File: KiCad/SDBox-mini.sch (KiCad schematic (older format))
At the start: 10 parts, among them J1 DB25_Male, J2 Micro_SD_Card, U1 ATmega328P-AU, Y1 Crystal_GND24_Small

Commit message: added 3V3 voltage regulator, added 74LVC125A buffer
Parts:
- added C1, C2: 10uF, Capacitor_SMD:C_1206_3216Metric_Pad1.42x1.75mm_HandSolder, symbol Device:C_Small
- added C3, C9: 0.1uF, Capacitor_SMD:C_0603_1608Metric_Pad1.05x0.95mm_HandSolder, symbol Device:C_Small
- added R2: 10k, Resistor_SMD:R_0603_1608Metric_Pad1.05x0.95mm_HandSolder, symbol Device:R_Small
- added U2: LM1117-3.3, Package_TO_SOT_SMD:SOT-223, symbol Regulator_Linear:LM1117-3.3
- added U3: 74LVC125A, Package_SO:TSSOP-14_4.4x5mm_P0.65mm, symbol SDBox-mini:74LVC125A
- Y1: footprint Oscillator:Oscillator_SMD_Fordahl_DFAS15-4Pin_5.0x3.2mm_HandSoldering -> SDBox-mini:Crystal_EuroQuartz_SMD_4Pin_5.0x3.2mm
- renumbered C1 to C4, C2 to C5, C3 to C6, C4 to C7, C5 to C8
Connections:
- net labels added: MISO_3V3, MOSI_3V3, SCK_3V3, SELECT_3V3
- net labels removed: CS
- wire segments 32 -> 37
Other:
- moved on the sheet: J1
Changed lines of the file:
@@
 $EndDescr
 $Comp
-L Device:C_Small C2
+L Device:C_Small C5
 U 1 1 606A3110
 P 3000 1600
-F 0 "C2" V 2850 1750 50  0000 R CNN
+F 0 "C5" V 2850 1750 50  0000 R CNN
 F 1 "0.1uF" V 2850 1400 50  0000 L CNN
 F 2 "Capacitor_SMD:C_0603_1608Metric_Pad1.05x0.95mm_HandSolder" H 3000 1600 50  0001 C CNN
@@
 L Connector:DB25_Male J1
 U 1 1 60F40974
-P 2500 2750
-F 0 "J1" V 2817 2750 50  0000 C CNN
-F 1 "DB25_Male" V 2726 2750 50  0000 C CNN
-F 2 "Connector_Dsub:DSUB-25_Male_EdgeMount_P2.77mm" H 2500 2750 50  0001 C CNN
-F 3 " ~" H 2500 2750 50  0001 C CNN
-	1    2500 2750
-	1    0    0    -1
-$EndComp
-Text GLabel 2200 1550 0    50   BiDi ~ 0
+P 2300 2750
+F 0 "J1" V 2617 2750 50  0000 C CNN
+F 1 "DB25_Male" V 2526 2750 50  0000 C CNN
+F 2 "Connector_Dsub:DSUB-25_Male_EdgeMount_P2.77mm" H 2300 2750 50  0001 C CNN
+F 3 " ~" H 2300 2750 50  0001 C CNN
+	1    2300 2750
+	1    0    0    -1
+$EndComp
+Text GLabel 2000 1550 0    50   BiDi ~ 0
 SELECT
-NoConn ~ 2200 1650
-NoConn ~ 2200 1850
-NoConn ~ 2200 2050
-Text GLabel 2200 1750 0    50   BiDi ~ 0
+NoConn ~ 2000 1650
+NoConn ~ 2000 1850
+NoConn ~ 2000 2050
+Text GLabel 2000 1750 0    50   BiDi ~ 0
 POUT
-Text GLabel 2200 1950 0    50   BiDi ~ 0
+Text GLabel 2000 1950 0    50   BiDi ~ 0
 BUSY
-Text GLabel 1850 2750 0    50   Input ~ 0
-GND
-Wire Wire Line
-	1850 2250 1850 2450
-Connection ~ 1850 2450
-Wire Wire Line
-	1850 2450 1850 2650
-Wire Wire Line
-	1850 3050 1850 2850
-Connection ~ 1850 2650
-Connection ~ 1850 2850
-Wire Wire Line
-	1850 2850 1850 2650
-Text GLabel 2200 2350 0    50   BiDi ~ 0
+Text GLabel 1650 2750 0    50   Input ~ 0
+GND
+Wire Wire Line
+	1650 2250 1650 2450
+Connection ~ 1650 2450
+Wire Wire Line
+	1650 2450 1650 2650
+Wire Wire Line
+	1650 3050 1650 2850
+Connection ~ 1650 2650
+Connection ~ 1650 2850
+Wire Wire Line
+	1650 2850 1650 2650
+Text GLabel 2000 2350 0    50   BiDi ~ 0
 D7
-Text GLabel 2200 2550 0    50   BiDi ~ 0
+Text GLabel 2000 2550 0    50   BiDi ~ 0
 D6
-Text GLabel 2200 2750 0    50   BiDi ~ 0
+Text GLabel 2000 2750 0    50   BiDi ~ 0
 D5
-Text GLabel 2200 2950 0    50   BiDi ~ 0
+Text GLabel 2000 2950 0    50   BiDi ~ 0
 D4
-Text GLabel 2200 3150 0    50   BiDi ~ 0
+Text GLabel 2000 3150 0    50   BiDi ~ 0
 D3
 Wire Wire Line
-	1850 3250 1850 3050
-Connection ~ 1850 3050
-Wire Wire Line
-	1850 2250 2200 2250
-Wire Wire Line
-	1850 2450 2200 2450
-Wire Wire Line
-	1850 2650 2200 2650
-Wire Wire Line
-	1850 2850 2200 2850
-Wire Wire Line
-	1850 3050 2200 3050
-Wire Wire Line
-	1850 3250 2200 3250
-Text GLabel 2200 3350 0    50   BiDi ~ 0
+	1650 3250 1650 3050
+Connection ~ 1650 3050
+Wire Wire Line
+	1650 2250 2000 2250
+Wire Wire Line
+	1650 2450 2000 2450
+Wire Wire Line
+	1650 2650 2000 2650
+Wire Wire Line
+	1650 2850 2000 2850
+Wire Wire Line
+	1650 3050 2000 3050
+Wire Wire Line
+	1650 3250 2000 3250
+Text GLabel 2000 3350 0    50   BiDi ~ 0
 D2
-Text GLabel 2200 3450 0    50   Output ~ 0
+Text GLabel 2000 3450 0    50   Output ~ 0
 RESET
-Text GLabel 2200 3550 0    50   BiDi ~ 0
+Text GLabel 2000 3550 0    50   BiDi ~ 0
 D1
-NoConn ~ 2200 3650
-Text GLabel 2200 3750 0    50   BiDi ~ 0
+NoConn ~ 2000 3650
+Text GLabel 2000 3750 0    50   BiDi ~ 0
 D0
 $Comp
@@
 	-1   0    0    1
 $EndComp
-NoConn ~ 2200 3850
+NoConn ~ 2000 3850
 Text GLabel 4950 2800 1    50   Input ~ 0
 VCC
@@
 F 0 "Y1" V 5300 2200 50  0000 L CNN
 F 1 "Crystal_GND24_Small" V 5500 2400 50  0001 L CNN
-F 2 "Oscillator:Oscillator_SMD_Fordahl_DFAS15-4Pin_5.0x3.2mm_HandSoldering" H 5300 2250 50  0001 C CNN
+F 2 "SDBox-mini:Crystal_EuroQuartz_SMD_4Pin_5.0x3.2mm" H 5300 2250 50  0001 C CNN
 F 3 "~" H 5300 2250 50  0001 C CNN
 	1    5300 2250
@@
 GND
 $Comp
-L Device:C_Small C4
+L Device:C_Small C7
 U 1 1 60FA06FB
 P 5550 2100
-F 0 "C4" V 5650 2250 50  0000 R CNN
+F 0 "C7" V 5650 2250 50  0000 R CNN
 F 1 "16pF" V 5650 1900 50  0000 L CNN
 F 2 "Capacitor_SMD:C_0603_1608Metric_Pad1.05x0.95mm_HandSolder" H 5550 2100 50  0001 C CNN
@@
 	4900 2100 5300 2100
 $Comp
-L Device:C_Small C5
+L Device:C_Small C8
 U 1 1 60FA5116
 P 5550 2400
-F 0 "C5" V 5450 2550 50  0000 R CNN
+F 0 "C8" V 5450 2550 50  0000 R CNN
 F 1 "16pF" V 5450 2200 50  0000 L CNN
 F 2 "Capacitor_SMD:C_0603_1608Metric_Pad1.05x0.95mm_HandSolder" H 5550 2400 50  0001 C CNN
@@
 Connection ~ 5650 2250
 $Comp
-L Device:C_Small C3
+L Device:C_Small C6
 U 1 1 60FA7C64
 P 3700 1250
-F 0 "C3" V 3800 1400 50  0000 R CNN
+F 0 "C6" V 3800 1400 50  0000 R CNN
 F 1 "0.1uF" V 3800 1050 50  0000 L CNN
 F 2 "Capacitor_SMD:C_0603_1608Metric_Pad1.05x0.95mm_HandSolder" H 3700 1250 50  0001 C CNN
@@
 Text GLabel 4550 3400 2    50   Output ~ 0
 TXO
-NoConn ~ 2200 2150
-NoConn ~ 2200 3950
+NoConn ~ 2000 2150
+NoConn ~ 2000 3950
 Text GLabel 4550 2000 2    50   Input ~ 0
 MISO
@@
 DTR
 $Comp
-L Device:C_Small C1
+L Device:C_Small C4
 U 1 1 60F8E9CC
 P 5350 3100
-F 0 "C1" V 5200 3250 50  0000 R CNN
+F 0 "C4" V 5200 3250 50  0000 R CNN
 F 1 "0.1uF" V 5200 2900 50  0000 L CNN
 F 2 "Capacitor_SMD:C_0603_1608Metric_Pad1.05x0.95mm_HandSolder" H 5350 3100 50  0001 C CNN
@@
 $EndComp
 NoConn ~ 7900 2350
-Text GLabel 7900 1750 2    50   Output ~ 0
+Text GLabel 7450 4800 2    50   Output ~ 0
 MISO
 Text GLabel 7900 1850 2    50   Input ~ 0
 GND
-Text GLabel 7900 1950 2    50   Input ~ 0
+Text GLabel 6550 3800 0    50   Input ~ 0
 SCK
 Text GLabel 7900 2050 2    50   Input ~ 0
 3V3
-Text GLabel 7900 2150 2    50   Input ~ 0
+Text GLabel 6550 3300 0    50   Input ~ 0
 MOSI
 NoConn ~ 7900 1650
 NoConn ~ 6200 1450
 Text GLabel 7900 2250 2    50   Input ~ 0
-CS
+SELECT_3V3
+$Comp
+L SDBox-mini:74LVC125A U3
+U 1 1 60FFE391
+P 7000 4150
+F 0 "U3" H 7000 5565 50  0000 C CNN
+F 1 "74LVC125A" H 7000 5474 50  0000 C CNN
+F 2 "Package_SO:TSSOP-14_4.4x5mm_P0.65mm" H 8200 5200 50  0001 C CNN
+F 3 "https://assets.nexperia.com/documents/data-sheet/74LVC125A.pdf" H 8200 5200 50  0001 C CNN
+	1    7000 4150
+	1    0    0    -1
+$EndComp
+Text GLabel 6550 3550 0    50   Input ~ 0
+GND
+Text GLabel 6550 4050 0    50   Input ~ 0
+GND
+Text GLabel 6550 4550 0    50   Input ~ 0
+GND
+Text GLabel 6550 5050 0    50   Input ~ 0
+GND
+Text GLabel 6550 4300 0    50   Input ~ 0
+SELECT
+Text GLabel 7450 4300 2    50   Output ~ 0
+SELECT_3V3
+Text GLabel 7450 4050 2    50   Input ~ 0
+GND
+$Comp
+L Device:C_Small C9
+U 1 1 61017825
+P 7450 5150
+F 0 "C9" H 7350 5150 50  0000 R CNN
+F 1 "0.1uF" H 7200 5250 50  0000 L CNN
+F 2 "Capacitor_SMD:C_0603_1608Metric_Pad1.05x0.95mm_HandSolder" H 7450 5150 50  0001 C CNN
+F 3 "~" H 7450 5150 50  0001 C CNN
+	1    7450 5150
+	-1   0    0    1
+$EndComp
+Text GLabel 7450 5250 3    50   Input ~ 0
+GND
+Text GLabel 7450 5050 2    50   Input ~ 0
+VCC
+$Comp
+L Device:R_Small R2
+U 1 1 6101E2BD
+P 6000 4700
+F 0 "R2" H 5941 4654 50  0000 R CNN
+F 1 "10k" H 5941 4745 50  0000 R CNN
+F 2 "Resistor_SMD:R_0603_1608Metric_Pad1.05x0.95mm_HandSolder" H 6000 4700 50  0001 C CNN
+F 3 "~" H 6000 4700 50  0001 C CNN
+	1    6000 4700
+	-1   0    0    1
+$EndComp
+Text GLabel 6000 4600 1    50   Input ~ 0
+3V3
+Text GLabel 7900 2150 2    50   Input ~ 0
+MOSI_3V3
+Text GLabel 7450 3300 2    50   Output ~ 0
+MOSI_3V3
+Text GLabel 7900 1750 2    50   Output ~ 0
+MISO_3V3
+Text GLabel 5700 4800 0    50   Input ~ 0
+MISO_3V3
+Wire Wire Line
+	5700 4800 6000 4800
+Connection ~ 6000 4800
+Wire Wire Line
+	6000 4800 6550 4800
+Text GLabel 7450 3800 2    50   Output ~ 0
+SCK_3V3
+Text GLabel 7900 1950 2    50   Input ~ 0
+SCK_3V3
+$Comp
+L Regulator_Linear:LM1117-3.3 U2
+U 1 1 61034FEA
+P 9550 1750
+F 0 "U2" H 9550 1992 50  0000 C CNN
+F 1 "LM1117-3.3" H 9550 1901 50  0000 C CNN
+F 2 "Package_TO_SOT_SMD:SOT-223" H 9550 1750 50  0001 C CNN
+F 3 "http://www.ti.com/lit/ds/symlink/lm1117.pdf" H 9550 1750 50  0001 C CNN
+	1    9550 1750
+	1    0    0    -1
+$EndComp
+Text GLabel 9250 1750 0    50   Input ~ 0
+VCC
+$Comp
+L Device:C_Small C1
+U 1 1 610421CE
+P 9250 1650
+F 0 "C1" H 9450 1650 50  0000 R CNN
+F 1 "10uF" H 9300 1550 50  0000 L CNN
+F 2 "Capacitor_SMD:C_1206_3216Metric_Pad1.42x1.75mm_HandSolder" H 9250 1650 50  0001 C CNN
+F 3 "~" H 9250 1650 50  0001 C CNN
+	1    9250 1650
+	-1   0    0    1
+$EndComp
+$Comp
+L Device:C_Small C2
+U 1 1 610444D0
+P 9850 1650
+F 0 "C2" H 9750 1650 50  0000 R CNN
+F 1 "10uF" H 9600 1550 50  0000 L CNN
+F 2 "Capacitor_SMD:C_1206_3216Metric_Pad1.42x1.75mm_HandSolder" H 9850 1650 50  0001 C CNN
+F 3 "~" H 9850 1650 50  0001 C CNN
+	1    9850 1650
+	-1   0    0    1
+$EndComp
+Text GLabel 9250 1550 1    50   Input ~ 0
+GND
+Text GLabel 9850 1550 1    50   Input ~ 0
+GND
+$Comp
+L Device:C_Small C3
+U 1 1 6104580B
+P 10200 1650
+F 0 "C3" H 10100 1650 50  0000 R CNN
+F 1 "0.1uF" H 9950 1550 50  0000 L CNN
+F 2 "Capacitor_SMD:C_0603_1608Metric_Pad1.05x0.95mm_HandSolder" H 10200 1650 50  0001 C CNN
+F 3 "~" H 10200 1650 50  0001 C CNN
+	1    10200 1650
+	-1   0    0    1
+$EndComp
+Text GLabel 10200 1550 1    50   Input ~ 0
+GND
+Wire Wire Line
+	9850 1750 10200 1750
+Connection ~ 9850 1750
+Wire Wire Line
+	9850 1850 9850 1750
+Text GLabel 9550 2050 3    50   Input ~ 0
+GND
+Text GLabel 10350 1750 2    50   Output ~ 0
+3V3
+Wire Wire Line
+	10200 1750 10350 1750
+Connection ~ 10200 1750
 $EndSCHEMATC

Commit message: added FTDI header
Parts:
- added J2: Conn_01x06, Connector_PinHeader_2.54mm:PinHeader_1x06_P2.54mm_Vertical, symbol Connector_Generic:Conn_01x06
- renumbered J2 to J3
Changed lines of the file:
@@
 NoConn ~ 4550 1800
 $Comp
-L Connector:Micro_SD_Card J2
+L Connector:Micro_SD_Card J3
 U 1 1 60FD5546
 P 7000 2050
-F 0 "J2" H 6950 1233 50  0000 C CNN
+F 0 "J3" H 6950 1233 50  0000 C CNN
 F 1 "Micro_SD_Card" H 6950 1324 50  0000 C CNN
 F 2 "SDBox-mini:GCT-MEM2055-00-190-01-A" H 8150 2350 50  0001 C CNN
@@
 GND
 Text GLabel 7450 5050 2    50   Input ~ 0
-VCC
+3V3
 $Comp
 L Device:R_Small R2
@@
 	10200 1750 10350 1750
 Connection ~ 10200 1750
+$Comp
+L Connector_Generic:Conn_01x06 J2
+U 1 1 6104A5C2
+P 2200 5000
+F 0 "J2" H 2118 4475 50  0000 C CNN
+F 1 "Conn_01x06" H 2118 4566 50  0000 C CNN
+F 2 "Connector_PinHeader_2.54mm:PinHeader_1x06_P2.54mm_Vertical" H 2200 5000 50  0001 C CNN
+F 3 "~" H 2200 5000 50  0001 C CNN
+	1    2200 5000
+	-1   0    0    1
+$EndComp
+Text GLabel 2400 5200 2    50   Input ~ 0
+DTR
+Text GLabel 2400 5100 2    50   Input ~ 0
+TXO
+Text GLabel 2400 5000 2    50   Output ~ 0
+RXI
+Text GLabel 2400 4900 2    50   Input ~ 0
+VCC
+Text GLabel 2400 4800 2    50   Input ~ 0
+GND
+Text GLabel 2400 4700 2    50   Input ~ 0
+GND
 $EndSCHEMATC

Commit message: changed to 74LVC3G17
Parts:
- removed U3: 74LVC125A, Package_SO:TSSOP-14_4.4x5mm_P0.65mm, symbol SDBox-mini:74LVC125A
- added U3: 74LVC3G17, Package_SO:TSSOP-8_3x3mm_P0.65mm, symbol SDBox-mini:74LVC3G17
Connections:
- wire segments 37 -> 39
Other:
- moved on the sheet: C9, R2
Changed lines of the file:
@@
 $EndComp
 NoConn ~ 7900 2350
-Text GLabel 7450 4800 2    50   Output ~ 0
+Text GLabel 6100 4250 2    50   Output ~ 0
 MISO
 Text GLabel 7900 1850 2    50   Input ~ 0
 GND
-Text GLabel 6550 3800 0    50   Input ~ 0
+Text GLabel 7650 4150 2    50   Input ~ 0
 SCK
 Text GLabel 7900 2050 2    50   Input ~ 0
 3V3
-Text GLabel 6550 3300 0    50   Input ~ 0
+Text GLabel 6850 3450 0    50   Input ~ 0
 MOSI
 NoConn ~ 7900 1650
@@
 Text GLabel 7900 2250 2    50   Input ~ 0
 SELECT_3V3
-$Comp
-L SDBox-mini:74LVC125A U3
-U 1 1 60FFE391
-P 7000 4150
-F 0 "U3" H 7000 5565 50  0000 C CNN
-F 1 "74LVC125A" H 7000 5474 50  0000 C CNN
-F 2 "Package_SO:TSSOP-14_4.4x5mm_P0.65mm" H 8200 5200 50  0001 C CNN
-F 3 "https://assets.nexperia.com/documents/data-sheet/74LVC125A.pdf" H 8200 5200 50  0001 C CNN
-	1    7000 4150
-	1    0    0    -1
-$EndComp
-Text GLabel 6550 3550 0    50   Input ~ 0
+Text GLabel 6800 4500 0    50   Input ~ 0
 GND
-Text GLabel 6550 4050 0    50   Input ~ 0
+Text GLabel 6850 4150 0    50   Input ~ 0
+SELECT
+Text GLabel 7650 4500 2    50   Output ~ 0
+SELECT_3V3
+Text GLabel 7850 3250 1    50   Input ~ 0
 GND
-Text GLabel 6550 4550 0    50   Input ~ 0
-GND
-Text GLabel 6550 5050 0    50   Input ~ 0
-GND
-Text GLabel 6550 4300 0    50   Input ~ 0
-SELECT
-Text GLabel 7450 4300 2    50   Output ~ 0
-SELECT_3V3
-Text GLabel 7450 4050 2    50   Input ~ 0
-GND
-$Comp
-L Device:C_Small C9
-U 1 1 61017825
-P 7450 5150
-F 0 "C9" H 7350 5150 50  0000 R CNN
-F 1 "0.1uF" H 7200 5250 50  0000 L CNN
-F 2 "Capacitor_SMD:C_0603_1608Metric_Pad1.05x0.95mm_HandSolder" H 7450 5150 50  0001 C CNN
-F 3 "~" H 7450 5150 50  0001 C CNN
-	1    7450 5150
-	-1   0    0    1
-$EndComp
-Text GLabel 7450 5250 3    50   Input ~ 0
-GND
-Text GLabel 7450 5050 2    50   Input ~ 0
-3V3
 $Comp
 L Device:R_Small R2
 U 1 1 6101E2BD
-P 6000 4700
-F 0 "R2" H 5941 4654 50  0000 R CNN
-F 1 "10k" H 5941 4745 50  0000 R CNN
-F 2 "Resistor_SMD:R_0603_1608Metric_Pad1.05x0.95mm_HandSolder" H 6000 4700 50  0001 C CNN
-F 3 "~" H 6000 4700 50  0001 C CNN
-	1    6000 4700
+P 5550 4500
+F 0 "R2" H 5491 4454 50  0000 R CNN
+F 1 "10k" H 5491 4545 50  0000 R CNN
+F 2 "Resistor_SMD:R_0603_1608Metric_Pad1.05x0.95mm_HandSolder" H 5550 4500 50  0001 C CNN
+F 3 "~" H 5550 4500 50  0001 C CNN
+	1    5550 4500
 	-1   0    0    1
 $EndComp
-Text GLabel 6000 4600 1    50   Input ~ 0
+Text GLabel 5550 4400 1    50   Input ~ 0
 3V3
 Text GLabel 7900 2150 2    50   Input ~ 0
 MOSI_3V3
-Text GLabel 7450 3300 2    50   Output ~ 0
+Text GLabel 7650 3800 2    50   Output ~ 0
 MOSI_3V3
 Text GLabel 7900 1750 2    50   Output ~ 0
 MISO_3V3
-Text GLabel 5700 4800 0    50   Input ~ 0
+Text GLabel 5250 4600 0    50   Input ~ 0
 MISO_3V3
 Wire Wire Line
-	5700 4800 6000 4800
-Connection ~ 6000 4800
+	5250 4600 5550 4600
+Connection ~ 5550 4600
 Wire Wire Line
-	6000 4800 6550 4800
-Text GLabel 7450 3800 2    50   Output ~ 0
+	5550 4600 6100 4600
+Text GLabel 6850 3800 0    50   Output ~ 0
 SCK_3V3
 Text GLabel 7900 1950 2    50   Input ~ 0
@@
 Text GLabel 2400 4700 2    50   Input ~ 0
 GND
+$Comp
+L Device:C_Small C9
+U 1 1 61017825
+P 7850 3350
+F 0 "C9" H 7700 3250 50  0000 R CNN
+F 1 "0.1uF" H 7500 3350 50  0000 L CNN
+F 2 "Capacitor_SMD:C_0603_1608Metric_Pad1.05x0.95mm_HandSolder" H 7850 3350 50  0001 C CNN
+F 3 "~" H 7850 3350 50  0001 C CNN
+	1    7850 3350
+	-1   0    0    1
+$EndComp
+$Comp
+L SDBox-mini:74LVC3G17 U3
+U 1 1 610573DA
+P 7250 4000
+F 0 "U3" H 7250 4915 50  0000 C CNN
+F 1 "74LVC3G17" H 7250 4824 50  0000 C CNN
+F 2 "Package_SO:TSSOP-8_3x3mm_P0.65mm" H 8100 4400 50  0001 C CNN
+F 3 "http://www.ti.com/lit/sg/scyt129e/scyt129e.pdf" H 8100 4400 50  0001 C CNN
+	1    7250 4000
+	1    0    0    -1
+$EndComp
+Text GLabel 8100 3450 2    50   Input ~ 0
+3V3
+Wire Wire Line
+	8100 3450 7850 3450
+Connection ~ 7850 3450
+Wire Wire Line
+	7850 3450 7700 3450
 $EndSCHEMATC

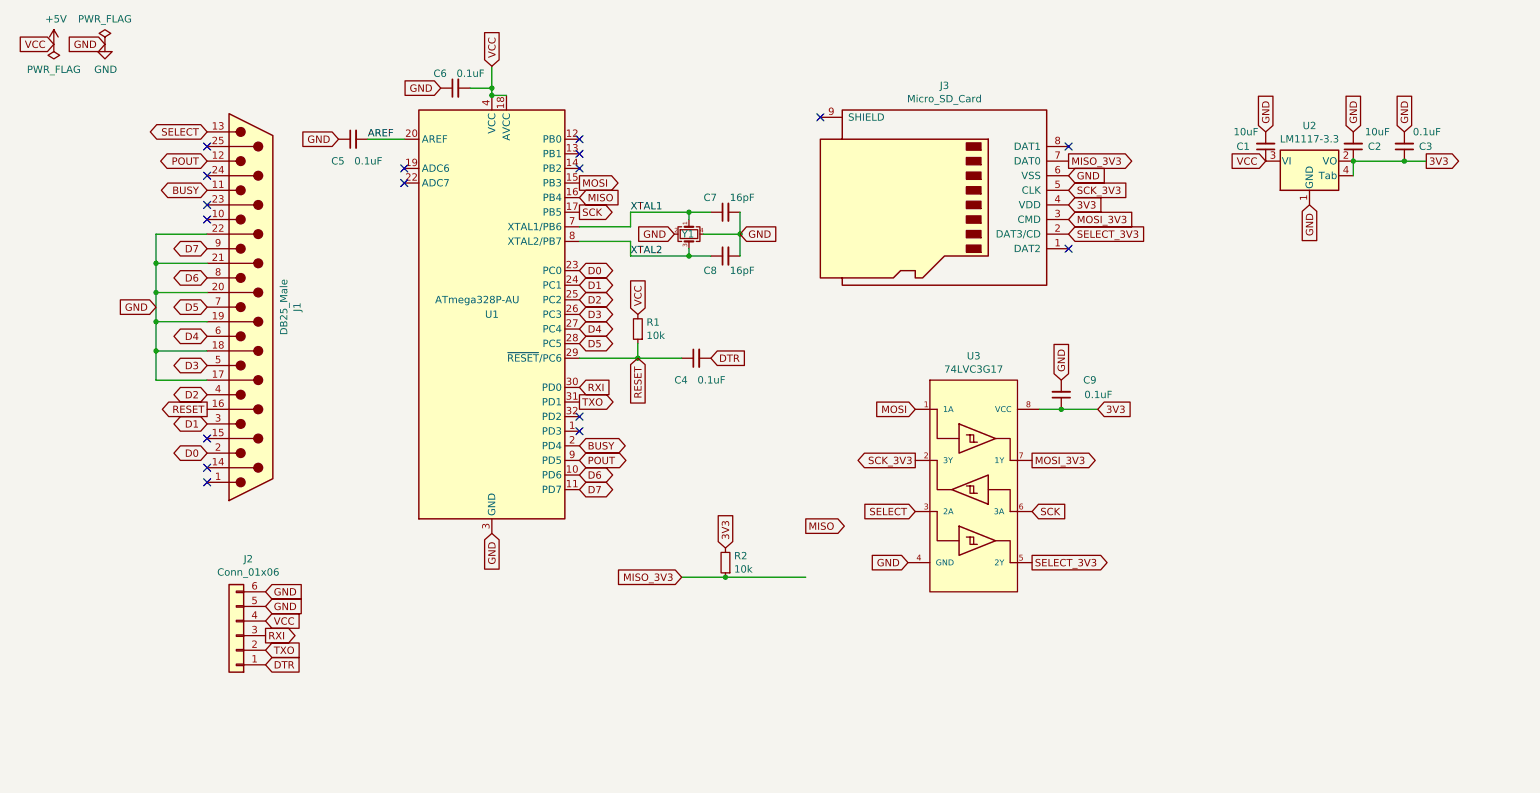
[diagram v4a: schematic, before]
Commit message: added USB micro jack, and Dual non-inverting Schmitt trigger, and debounce circuit for card detect
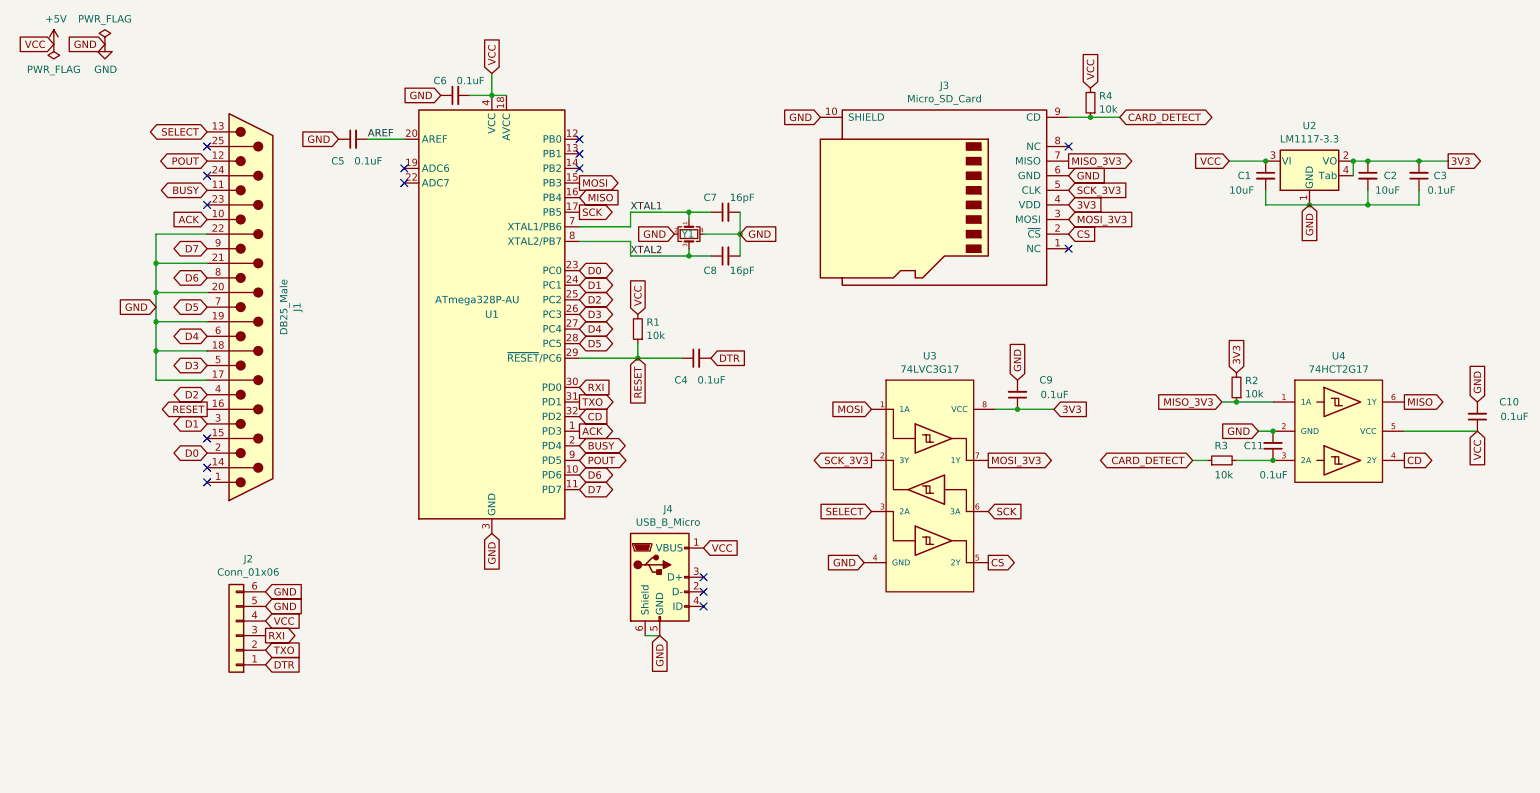
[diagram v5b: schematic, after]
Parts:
- removed J3: Micro_SD_Card, SDBox-mini:GCT-MEM2055-00-190-01-A, symbol Connector:Micro_SD_Card
- added C10, C11: 0.1uF, Capacitor_SMD:C_0603_1608Metric_Pad1.05x0.95mm_HandSolder, symbol Device:C_Small
- added J3: Micro_SD_Card, SDBox-mini:GCT-MEM2055-00-190-01-A, symbol SDBox-mini:Micro_SD_Card
- added J4: USB_B_Micro, SDBox-mini:USB_Micro-B_Unknown_5s_SMT, symbol Connector:USB_B_Micro
- added R3, R4: 10k, Resistor_SMD:R_0603_1608Metric_Pad1.05x0.95mm_HandSolder, symbol Device:R_Small
- added U4: 74HCT2G17, Package_SO:TSOP-6_1.65x3.05mm_P0.95mm, symbol SDBox-mini:74HCT2G17
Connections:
- net labels added: ACK, CARD_DETECT, CD, CS
- net labels removed: SELECT_3V3
- wire segments 39 -> 53
- no-connect marks 17 -> 16
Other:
- moved on the sheet: C1, C2, C3, C6, C9, R2, U3
